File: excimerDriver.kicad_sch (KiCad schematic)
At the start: 38 parts, among them IC3 INA210, IC6 STM32G071KBT6, J1 B08B-XASK-1-A_LF__SN_, J2 TC2050-IDC, J3 BM02B-SRSS-TB_LF__SN_, J4 BM02B-SRSS-TB_LF__SN_, J6 640445-2, Q3 BSS138

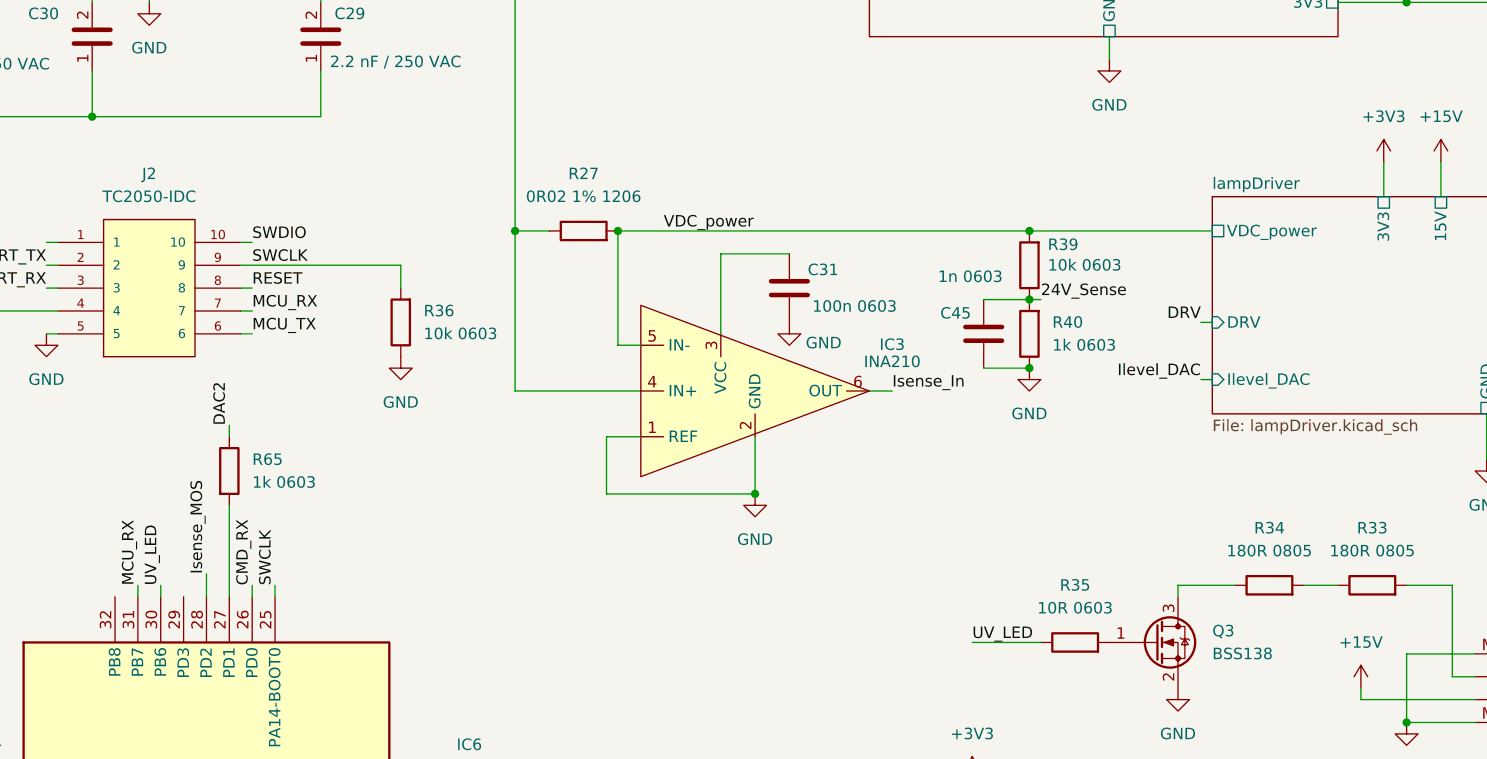
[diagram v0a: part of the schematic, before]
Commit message: new current control V1
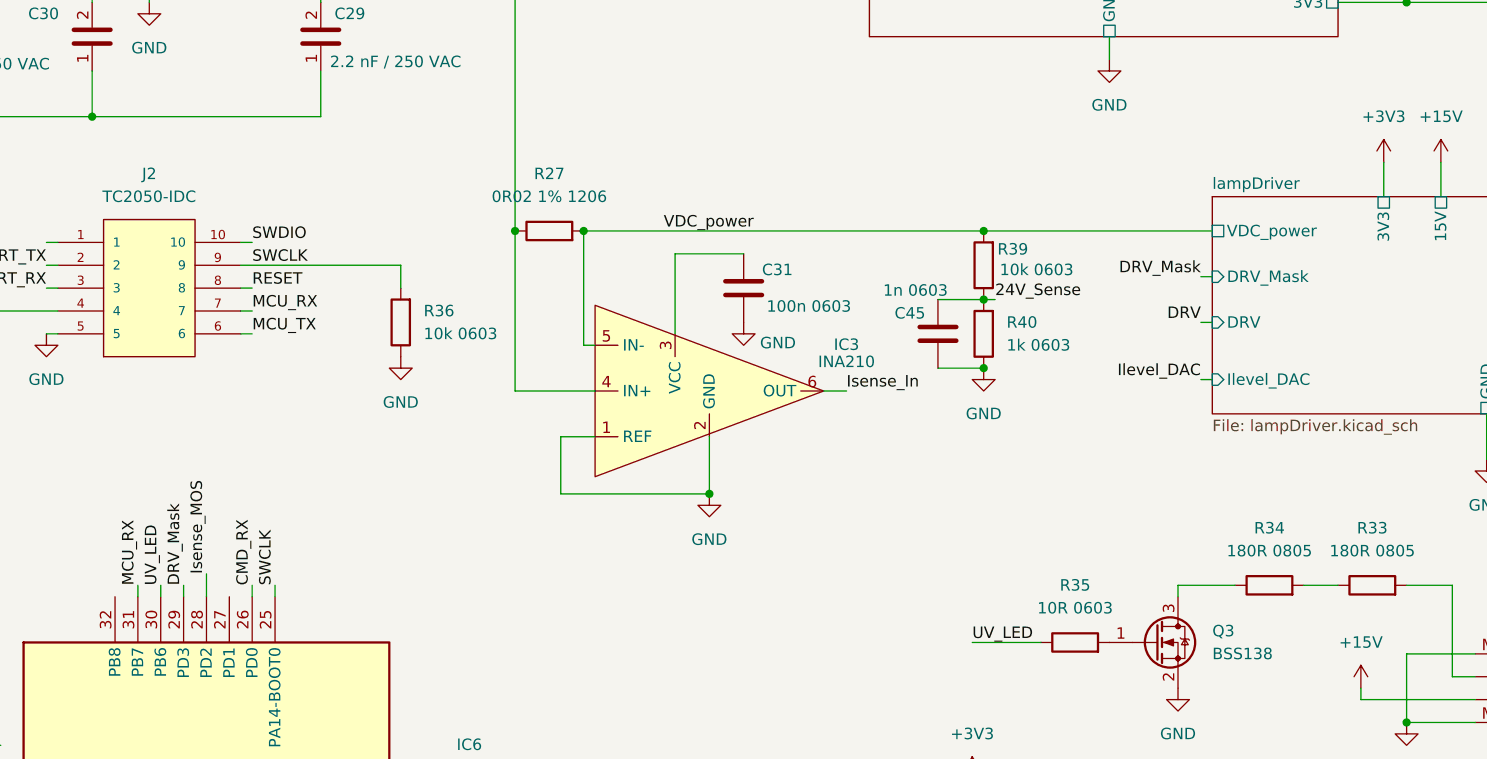
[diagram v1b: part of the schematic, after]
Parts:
- removed R65: 1k 0603, Resistor_SMD:R_0603_1608Metric, symbol Device:R
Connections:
- net DRV_Mask: now reaches IC6.29 (PD3)
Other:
- sheet lampDriver ports: added DRV_Mask; removed none
- moved on the sheet: C31, C45, IC3, R27, R39, R40

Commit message: 251704 end of day
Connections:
- net +3V3: now also C31.1, IC3.3 (VCC)
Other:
- moved on the sheet: C31, IC3
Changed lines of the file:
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@@
 	)
 	(junction
+		(at 148.59 77.47)
+		(diameter 0)
+		(color 0 0 0 0)
+	)
+	(junction
 		(at 43.18 148.59)
 		(diameter 0)
@@
 	)
 	(junction
-		(at 151.13 92.71)
+		(at 152.4 104.14)
 		(diameter 0)
 		(color 0 0 0 0)
@@
 	(wire
 		(pts
-			(xy 151.13 86.36) (xy 151.13 92.71)
+			(xy 152.4 97.79) (xy 152.4 104.14)
 		)
 		(stroke
@@
 	(wire
 		(pts
-			(xy 137.16 76.2) (xy 138.43 76.2)
+			(xy 137.16 87.63) (xy 139.7 87.63)
 		)
 		(stroke
@@
 	(wire
 		(pts
-			(xy 137.16 63.5) (xy 137.16 76.2)
+			(xy 137.16 63.5) (xy 137.16 87.63)
 		)
 		(stroke
@@
 	(wire
 		(pts
-			(xy 147.32 66.04) (xy 154.94 66.04)
+			(xy 148.59 77.47) (xy 156.21 77.47)
 		)
 		(stroke
@@
 	(wire
 		(pts
-			(xy 134.62 86.36) (xy 134.62 92.71)
+			(xy 135.89 97.79) (xy 135.89 104.14)
 		)
 		(stroke
@@
 	(wire
 		(pts
-			(xy 147.32 74.93) (xy 147.32 66.04)
+			(xy 148.59 86.36) (xy 148.59 77.47)
 		)
 		(stroke
@@
 	(wire
 		(pts
-			(xy 134.62 92.71) (xy 151.13 92.71)
+			(xy 135.89 104.14) (xy 152.4 104.14)
 		)
 		(stroke
@@
 	(wire
 		(pts
-			(xy 138.43 86.36) (xy 134.62 86.36)
+			(xy 139.7 97.79) (xy 135.89 97.79)
 		)
 		(stroke
@@
 	(wire
 		(pts
-			(xy 129.54 81.28) (xy 138.43 81.28)
+			(xy 129.54 92.71) (xy 139.7 92.71)
 		)
 		(stroke
@@
 	(wire
 		(pts
-			(xy 129.54 63.5) (xy 129.54 81.28)
+			(xy 129.54 63.5) (xy 129.54 92.71)
 		)
 		(stroke
@@
 	(wire
 		(pts
-			(xy 163.83 81.28) (xy 166.37 81.28)
+			(xy 165.1 92.71) (xy 167.64 92.71)
 		)
 		(stroke
@@
 			"UFgAAAAAMSgsAAAAgBgUFgAAAEAMCgsAAAAgBoUFAAAAEIPCAgAAAIhBYQEAAADEoLAAAAAAYlBY"
 			"AAAAADEoLAAAAIAYFBYAAABADAoLAAAAIAaFBQAAABCDwgIAAACIQWEBAAAAxKCwAAAAAGL+FzCI"
-			"XY5DdsKkAAAAAElFTkSuQmCC"
+			"XY5DdsKkAAAAAElFTkSuQmCC+P////////9IxoOeIgEAAPj/////////KM6DniIBAAD4////////"
+			"/7jOg54iAQAA+P////////8EAAAAIgEAAPj/////////AAAAACIBAAD4/////////3id7MoiAQAA"
+			"+P////////8EAAAAIgEAAPj/////////QOn1lSIBAAD4/////////wQAAAAiAQAA+P////////9o"
+			"0IOeIgEAAPj/////////cOv1lSIBAAD4//////////DS9ZUiAQAA+P////////8EAAAAIgEAAPj/"
+			"////////BAAAACIBAAD4/////////wQAAAAiAQAA+P////////8AAAAAIgEAAPj/////////QNv1"
+			"lSIBAAD4//////////Dn9ZUiAQAA+P////////8A3fWVIgEAAPj/////////BAAAACIBAAD4////"
+			"/////8De9ZUiAQAA+P////////8EAAAAIgEAAPj/////////BAAAACIBAAD4/////////wQAAAAi"
+			"AQAA+P////////+CBAAAIgEAAPj/////////BAAAACIBAAD4/////////+h97MoiAQAA+P//////"
+			"//8EAAAAIgEAAPj/////////BAAAACIBAAD4/////////zDR9ZUiAQAA+P////////8EAAAAIgEA"
+			"APj/////////BAAAACIBAAD4/////////8De9ZUiAQAA+P////////8EAAAAIgEAAPj/////////"
+			"IOr1lSIBAAD4/////////yDq9ZUiAQAA+P////////8EAAAAIgEAAPj/////////BAAAACIBAAD4"
+			"/////////8DQ9ZUiAQAA+P////////8EAAAAIgEAAPj/////////BAAAACIBAAD4/////////wQA"
+			"AAAiAQAA+P////////8AAAAAIgEAAPj/////////OLiDniIBAAD4/////////wQAAAAiAQAA+P//"
+			"//////9Q5fWVIgEAAPj/////////MAQAACIBAAD4/////////1i5g54iAQAA+P////////8EAAAA"
+			"IgEAAPj/////////aIDsyiIBAAD4/////////wQAAAAiAQAA+P////////8EAAAAIgEAAPj/////"
+			"////CJ/syiIBAAD4/////////wQAAAAiAQAA+P////////8oczLTIgEAAPj/////////BAAAACIB"
+			"AAD4/////////yhzMtMiAQAA+P////////8EAAAAIgEAAPj/////////BAAAACIBAAD4////////"
+			"/yhzMtMiAQAA+P////////8EAAAAIgEAAPj/////////KHMy0yIBAAD4/////////yhzMtMiAQAA"
+			"+P////////8EAAAAIgEAAA=="
 		)
 	)
@@
 	)
 	(label "Isense_In"
-		(at 166.37 81.28 0)
+		(at 167.64 92.71 0)
 		(effects
 			(font
@@
 	(symbol
 		(lib_id "power:GND")
-		(at 154.94 73.66 0)
+		(at 156.21 85.09 0)
 		(unit 1)
 		(exclude_from_sim no)
@@
 		(dnp no)
 		(property "Reference" "#PWR030"
-			(at 154.94 80.01 0)
+			(at 156.21 91.44 0)
 			(hide yes)
 			(effects
@@
 		)
 		(property "Value" "GND"
-			(at 158.75 75.946 0)
+			(at 160.02 87.376 0)
 			(effects
 				(font
@@
 		)
 		(property "Footprint" ""
-			(at 154.94 73.66 0)
+			(at 156.21 85.09 0)
 			(hide yes)
 			(effects
@@
 		)
 		(property "Datasheet" ""
-			(at 154.94 73.66 0)
+			(at 156.21 85.09 0)
 			(hide yes)
 			(effects
@@
 		)
 		(property "Description" "Power symbol creates a global label with name \"GND\" , ground"
-			(at 154.94 73.66 0)
+			(at 156.21 85.09 0)
 			(hide yes)
 			(effects
@@
 	)
 	(symbol
+		(lib_id "power:+3V3")
+		(at 148.59 77.47 0)
+		(unit 1)
+		(exclude_from_sim no)
+		(in_bom yes)
+		(on_board yes)
+		(dnp no)
+		(fields_autoplaced yes)
+		(property "Reference" "#PWR082"
+			(at 148.59 81.28 0)
+			(hide yes)
+			(effects
+				(font
+					(size 1.27 1.27)
+				)
+			)
+		)
+		(property "Value" "+3V3"
+			(at 148.59 72.39 0)
+			(effects
+				(font
+					(size 1.27 1.27)
+				)
+			)
+		)
+		(property "Footprint" ""
+			(at 148.59 77.47 0)
+			(hide yes)
+			(effects
+				(font
+					(size 1.27 1.27)
+				)
+			)
+		)
+		(property "Datasheet" ""
+			(at 148.59 77.47 0)
+			(hide yes)
+			(effects
+				(font
+					(size 1.27 1.27)
+				)
+			)
+		)
+		(property "Description" "Power symbol creates a global label with name \"+3V3\""
+			(at 148.59 77.47 0)
+			(hide yes)
+			(effects
+				(font
+					(size 1.27 1.27)
+				)
+			)
+		)
+		(pin "1"
+		)
+		(instances
+			(project "OSLUV"
+				(path "/c6e900e0-9399-44f0-8089-9dd7b8ffe54c/9b3070c3-43e0-4d43-9da1-9bc1bd2d6fb9"
+					(reference "#PWR082")
+					(unit 1)
+				)
+			)
+		)
+	)
+	(symbol
 		(lib_id "power:GND")
 		(at 55.88 121.92 0)
@@
 	(symbol
 		(lib_id "Device:C")
-		(at 154.94 69.85 0)
+		(at 156.21 81.28 0)
 		(unit 1)
 		(exclude_from_sim no)
@@
 		(dnp no)
 		(property "Reference" "C31"
-			(at 156.972 67.818 0)
+			(at 158.242 79.248 0)
 			(effects
 				(font
@@
 		)
 		(property "Value" "100n 0603"
-			(at 157.48 71.882 0)
+			(at 158.75 83.312 0)
 			(effects
 				(font
@@
 		)
 		(property "Footprint" "Capacitor_SMD:C_0603_1608Metric"
-			(at 155.9052 73.66 0)
+			(at 157.1752 85.09 0)
 			(hide yes)
 			(effects
@@
 		)
 		(property "Datasheet" ""
-			(at 154.94 69.85 0)
+			(at 156.21 81.28 0)
 			(hide yes)
 			(effects
@@
 		)
 		(property "Description" "Unpolarized capacitor"
-			(at 154.94 69.85 0)
+			(at 156.21 81.28 0)
 			(hide yes)
 			(effects
@@
 	(symbol
 		(lib_id "power:GND")
-		(at 151.13 92.71 0)
+		(at 152.4 104.14 0)
 		(unit 1)
 		(exclude_from_sim no)
@@
 		(fields_autoplaced yes)
 		(property "Reference" "#PWR029"
-			(at 151.13 99.06 0)
+			(at 152.4 110.49 0)
 			(hide yes)
 			(effects
@@
 		)
 		(property "Value" "GND"
-			(at 151.13 97.79 0)
+			(at 152.4 109.22 0)
 			(effects
 				(font
@@
 		)
 		(property "Footprint" ""
-			(at 151.13 92.71 0)
+			(at 152.4 104.14 0)
 			(hide yes)
 			(effects
@@
 		)
 		(property "Datasheet" ""
-			(at 151.13 92.71 0)
+			(at 152.4 104.14 0)
 			(hide yes)
 			(effects
@@
 		)
 		(property "Description" "Power symbol creates a global label with name \"GND\" , ground"
-			(at 151.13 92.71 0)
+			(at 152.4 104.14 0)
 			(hide yes)
 			(effects
@@
 	(symbol
 		(lib_id "Hansmann:INA210")
-		(at 138.43 81.28 0)
+		(at 139.7 92.71 0)
 		(unit 1)
 		(exclude_from_sim no)
@@
 		(fields_autoplaced yes)
 		(property "Reference" "IC3"
-			(at 166.37 76.1298 0)
+			(at 167.64 87.5598 0)
 			(effects
 				(font
@@
 		)
 		(property "Value" "INA210"
-			(at 166.37 78.0349 0)
+			(at 167.64 89.4649 0)
 			(effects
 				(font
@@
 		)
 		(property "Footprint" "Hansmann:SOT95P280X90-6N"
-			(at 138.43 81.28 0)
+			(at 139.7 92.71 0)
 			(hide yes)
 			(effects
@@
 		)
 		(property "Datasheet" ""
-			(at 138.43 81.28 0)
+			(at 139.7 92.71 0)
 			(hide yes)
 			(effects
@@
 		)
 		(property "Description" ""
-			(at 138.43 81.28 0)
+			(at 139.7 92.71 0)
 			(hide yes)
 			(effects
